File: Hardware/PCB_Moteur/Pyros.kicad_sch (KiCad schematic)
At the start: 33 parts, among them J1 Screw_Terminal_01x04, U3 SI5442DU-T1-GE3, U7 SI5442DU-T1-GE3, U8 LM393

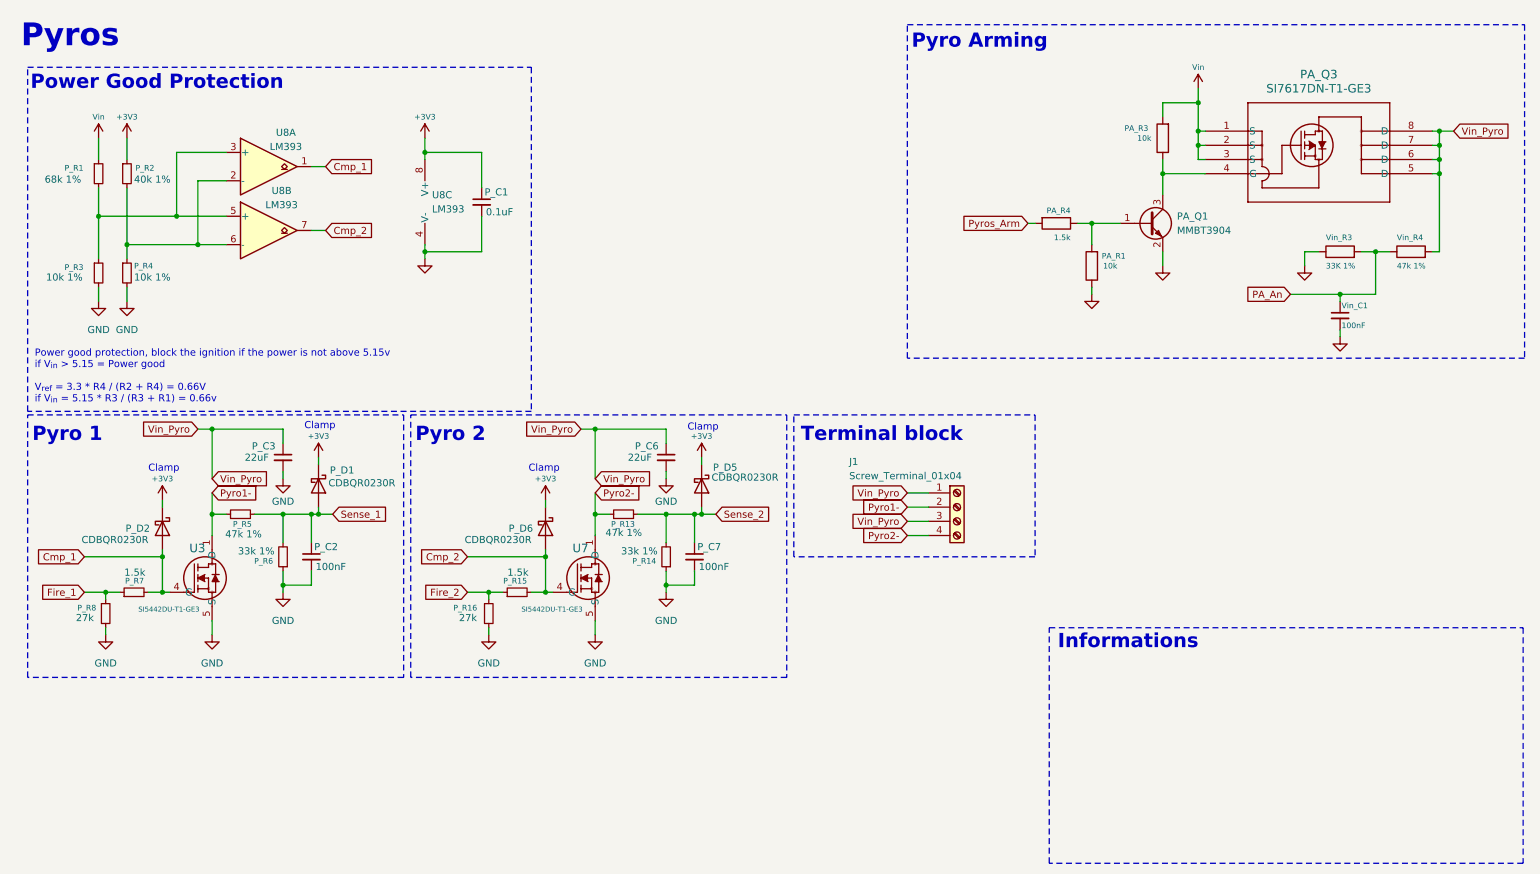
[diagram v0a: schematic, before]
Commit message: fix: LDO 5V SHDN + REFs (missing) + change EN valves controller connection + fix intrumental ampliop + add pull-down to sleep pins
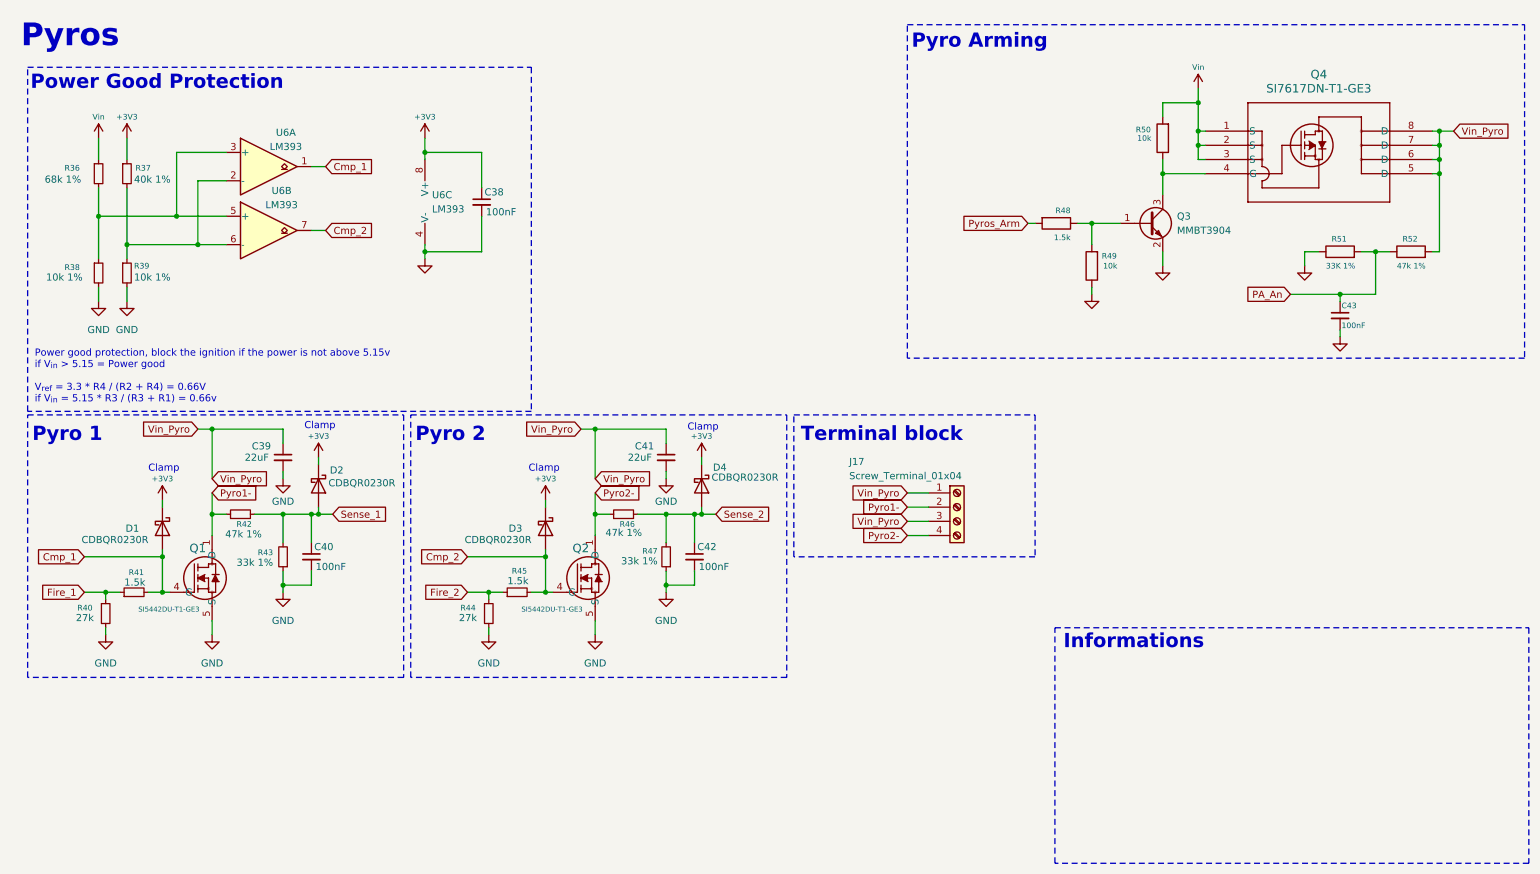
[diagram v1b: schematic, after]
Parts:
- C38: renamed from P_C1; value 0.1uF -> 100nF
- renumbered P_C3 to C39, P_C2 to C40, P_C6 to C41, P_C7 to C42, Vin_C1 to C43, P_D2 to D1, P_D1 to D2, P_D6 to D3, P_D5 to D4, J1 to J17, U3 to Q1, U7 to Q2, PA_Q1 to Q3, PA_Q3 to Q4, P_R1 to R36, P_R2 to R37, P_R3 to R38, P_R4 to R39, P_R8 to R40, P_R7 to R41, P_R5 to R42, P_R6 to R43, P_R16 to R44, P_R15 to R45, P_R13 to R46, P_R14 to R47, PA_R4 to R48, PA_R1 to R49, PA_R3 to R50, Vin_R3 to R51, Vin_R4 to R52, U8 to U6

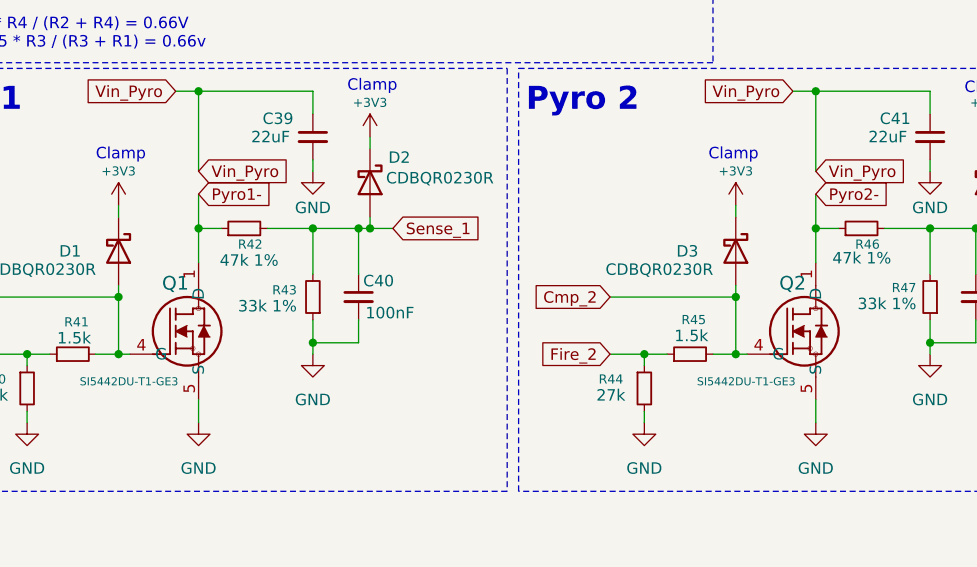
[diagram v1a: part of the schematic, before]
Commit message: wip : minor corrections and fix footprints except connectors
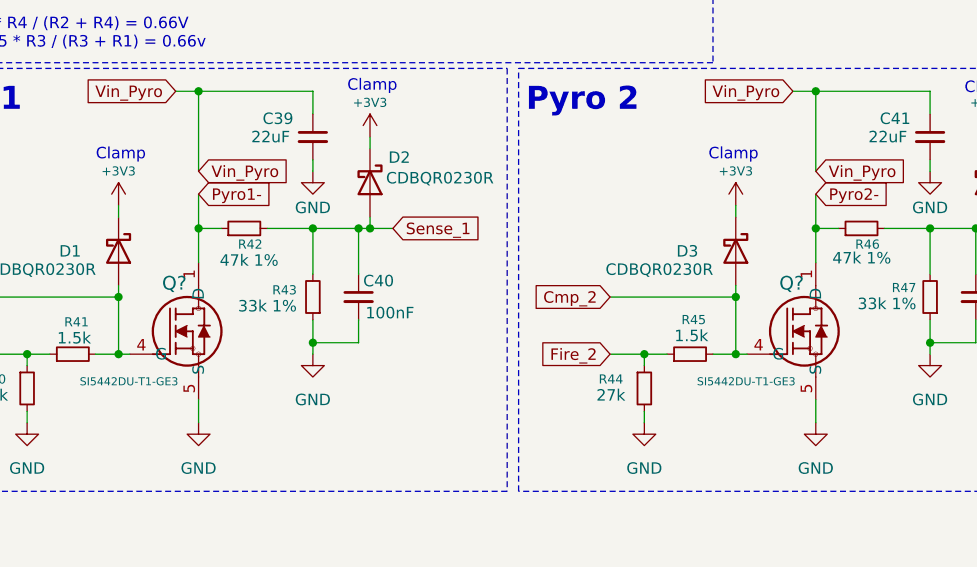
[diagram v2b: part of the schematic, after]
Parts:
- removed Q2: SI5442DU-T1-GE3, SON_8DU-T1-GE3_VIS, symbol ODB2:SI5442DU-T1-GE3
- added Q?: SI5442DU-T1-GE3, pcb_moteur:SON_8DU-T1-GE3_VIS, symbol ODB2:SI5442DU-T1-GE3
- C38, C39, C40, C41, C42, C43: footprint Capacitor_SMD:C_0603_1608Metric -> Capacitor_SMD:C_0805_2012Metric
- Q4: footprint ODB:POWERPAK_1212-8_VIS -> pcb_moteur:POWERPAK_1212-8_VIS
- Q?: renamed from Q1; footprint SON_8DU-T1-GE3_VIS -> pcb_moteur:SON_8DU-T1-GE3_VIS; DigiKey_Part_Number (none) -> SI5442DU-T1-GE3CT-ND; Manufacturer_Part_Number (none) -> SI5442DU-T1-GE3
- U6: footprint (none) -> Package_SO:SOIC-8_3.9x4.9mm_P1.27mm
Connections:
- net Cmp_2: now also Q?.4 (G)
- net GND: now also Q?.5 (S), Q?.9 (S)
- net Pyro2-: now also Q?.1 (D), Q?.10 (D), Q?.2 (D), Q?.3 (D), Q?.6 (D), Q?.7 (D), Q?.8 (D)
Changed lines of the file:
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@@
 	)
 	(symbol
-		(lib_id "ODB2:SI5442DU-T1-GE3")
-		(at 107.95 115.57 0)
-		(unit 1)
-		(exclude_from_sim no)
-		(in_bom yes)
-		(on_board yes)
-		(dnp no)
-		(property "Reference" "Q2"
-			(at 111.506 107.696 0)
-			(effects
-				(font
-					(size 1.524 1.524)
-				)
-				(justify left)
-			)
-		)
-		(property "Value" "SI5442DU-T1-GE3"
-			(at 102.362 118.618 0)
-			(effects
-				(font
-					(size 0.889 0.889)
-				)
-				(justify left)
-			)
-		)
-		(property "Footprint" "SON_8DU-T1-GE3_VIS"
-			(at 107.95 115.57 0)
-			(effects
-				(font
-					(size 1.27 1.27)
-					(italic yes)
-				)
-				(hide yes)
-			)
-		)
-		(property "Datasheet" "https://www.vishay.com/doc?63233"
-			(at 107.95 115.57 0)
-			(effects
-				(font
-					(size 1.27 1.27)
-					(italic yes)
-				)
-				(hide yes)
-			)
-		)
-		(property "Description" ""
-			(at 107.95 115.57 0)
-			(effects
-				(font
-					(size 1.27 1.27)
-				)
-				(hide yes)
-			)
-		)
-		(pin "4"
-		)
-		(pin "2"
-		)
-		(pin "3"
-		)
-		(pin "5"
-		)
-		(pin "1"
-		)
-		(pin "8"
-		)
-		(pin "7"
-		)
-		(pin "9"
-		)
-		(pin "6"
-		)
-		(pin "10"
-		)
-		(instances
-			(project "PCB_moteur"
-				(path "/b0d87684-7b1c-41d8-8358-755aa327573e/1c3f73a9-ace7-4654-9081-04f4c5cd0c08"
-					(reference "Q2")
-					(unit 1)
-				)
-			)
-		)
-	)
-	(symbol
 		(lib_id "power:GND")
 		(at 85.09 55.88 0)
@@
 			)
 		)
-		(property "Footprint" "Capacitor_SMD:C_0603_1608Metric"
+		(property "Footprint" "Capacitor_SMD:C_0805_2012Metric"
 			(at 59.69 91.44 0)
 			(effects
@@
 			)
 		)
-		(property "Footprint" "Capacitor_SMD:C_0603_1608Metric"
+		(property "Footprint" "Capacitor_SMD:C_0805_2012Metric"
 			(at 133.35 109.22 0)
 			(effects
@@
 			)
 		)
-		(property "Footprint" ""
+		(property "Footprint" "Package_SO:SOIC-8_3.9x4.9mm_P1.27mm"
 			(at 57.15 50.8 0)
 			(effects
@@
 			)
 		)
-		(property "Datasheet" "http://www.ti.com/lit/ds/symlink/lm393.pdf"
+		(property "Datasheet" "https://www.digikey.ca/en/products/detail/texas-instruments/LM393DR/276659"
 			(at 57.15 50.8 0)
 			(effects
@@
 			)
 		)
-		(property "Footprint" "Capacitor_SMD:C_0603_1608Metric"
+		(property "Footprint" "Capacitor_SMD:C_0805_2012Metric"
 			(at 248.92 66.04 0)
 			(effects
@@
 			)
 		)
-		(property "Footprint" ""
+		(property "Footprint" "Package_SO:SOIC-8_3.9x4.9mm_P1.27mm"
 			(at 57.15 39.37 0)
 			(effects
@@
 			)
 		)
-		(property "Datasheet" "http://www.ti.com/lit/ds/symlink/lm393.pdf"
+		(property "Datasheet" "https://www.digikey.ca/en/products/detail/texas-instruments/LM393DR/276659"
 			(at 57.15 39.37 0)
 			(effects
@@
 			)
 		)
-		(property "Footprint" "ODB:POWERPAK_1212-8_VIS"
+		(property "Footprint" "pcb_moteur:POWERPAK_1212-8_VIS"
 			(at 224.79 33.02 0)
 			(effects
@@
 			)
 		)
-		(property "Footprint" "Capacitor_SMD:C_0603_1608Metric"
+		(property "Footprint" "Capacitor_SMD:C_0805_2012Metric"
 			(at 64.77 109.22 0)
 			(effects
@@
 			)
 		)
-		(property "Footprint" ""
+		(property "Footprint" "Package_SO:SOIC-8_3.9x4.9mm_P1.27mm"
 			(at 87.63 45.72 0)
 			(effects
@@
 			)
 		)
-		(property "Datasheet" "http://www.ti.com/lit/ds/symlink/lm393.pdf"
+		(property "Datasheet" "https://www.digikey.ca/en/products/detail/texas-instruments/LM393DR/276659"
 			(at 87.63 45.72 0)
 			(effects
@@
 			)
 		)
-		(property "Footprint" "Capacitor_SMD:C_0603_1608Metric"
+		(property "Footprint" "Capacitor_SMD:C_0805_2012Metric"
 			(at 128.27 91.44 0)
 			(effects
@@
 		(lib_name "SI5442DU-T1-GE3_3")
 		(lib_id "ODB2:SI5442DU-T1-GE3")
+		(at 107.95 115.57 0)
+		(unit 1)
+		(exclude_from_sim no)
+		(in_bom yes)
+		(on_board yes)
+		(dnp no)
+		(property "Reference" "Q?"
+			(at 111.506 107.696 0)
+			(effects
+				(font
+					(size 1.524 1.524)
+				)
+				(justify left)
+			)
+		)
+		(property "Value" "SI5442DU-T1-GE3"
+			(at 102.362 118.618 0)
+			(effects
+				(font
+					(size 0.889 0.889)
+				)
+				(justify left)
+			)
+		)
+		(property "Footprint" "pcb_moteur:SON_8DU-T1-GE3_VIS"
+			(at 107.95 115.57 0)
+			(effects
+				(font
+					(size 1.27 1.27)
+					(italic yes)
+				)
+				(hide yes)
+			)
+		)
+		(property "Datasheet" "https://www.digikey.com/en/products/detail/vishay-siliconix/SI5442DU-T1-GE3/4142130"
+			(at 107.95 115.57 0)
+			(effects
+				(font
+					(size 1.27 1.27)
+					(italic yes)
+				)
+				(hide yes)
+			)
+		)
+		(property "Description" ""
+			(at 107.95 115.57 0)
+			(effects
+				(font
+					(size 1.27 1.27)
+				)
+				(hide yes)
+			)
+		)
+		(property "DigiKey_Part_Number" "SI5442DU-T1-GE3CT-ND"
+			(at 107.95 115.57 0)
+			(effects
+				(font
+					(size 1.27 1.27)
+				)
+				(hide yes)
+			)
+		)
+		(property "Purchase-URL" ""
+			(at 107.95 115.57 0)
+			(effects
+				(font
+					(size 1.27 1.27)
+				)
+				(hide yes)
+			)
+		)
+		(property "Sim.Device" ""
+			(at 107.95 115.57 0)
+			(effects
+				(font
+					(size 1.27 1.27)
+				)
+				(hide yes)
+			)
+		)
+		(property "Sim.Pins" ""
+			(at 107.95 115.57 0)
+			(effects
+				(font
+					(size 1.27 1.27)
+				)
+				(hide yes)
+			)
+		)
+		(property "Sim.Type" ""
+			(at 107.95 115.57 0)
+			(effects
+				(font
+					(size 1.27 1.27)
+				)
+				(hide yes)
+			)
+		)
+		(property "Manufacturer_Part_Number" "SI5442DU-T1-GE3"
+			(at 107.95 115.57 0)
+			(effects
+				(font
+					(size 1.27 1.27)
+				)
+				(hide yes)
+			)
+		)
+		(pin "4"
+		)
+		(pin "2"
+		)
+		(pin "3"
+		)
+		(pin "5"
+		)
+		(pin "1"
+		)
+		(pin "8"
+		)
+		(pin "7"
+		)
+		(pin "9"
+		)
+		(pin "6"
+		)
+		(pin "10"
+		)
+		(instances
+			(project "PCB_moteur"
+				(path "/b0d87684-7b1c-41d8-8358-755aa327573e/1c3f73a9-ace7-4654-9081-04f4c5cd0c08"
+					(reference "Q?")
+					(unit 1)
+				)
+			)
+		)
+	)
+	(symbol
+		(lib_name "SI5442DU-T1-GE3_3")
+		(lib_id "ODB2:SI5442DU-T1-GE3")
 		(at 39.37 115.57 0)
 		(unit 1)
@@
 		(on_board yes)
 		(dnp no)
-		(property "Reference" "Q1"
+		(property "Reference" "Q?"
 			(at 42.926 107.696 0)
 			(effects
@@
 			)
 		)
-		(property "Footprint" "SON_8DU-T1-GE3_VIS"
+		(property "Footprint" "pcb_moteur:SON_8DU-T1-GE3_VIS"
 			(at 39.37 115.57 0)
 			(effects
@@
 			)
 		)
-		(property "Datasheet" "https://www.vishay.com/doc?63233"
+		(property "Datasheet" "https://www.digikey.com/en/products/detail/vishay-siliconix/SI5442DU-T1-GE3/4142130"
 			(at 39.37 115.57 0)
 			(effects
@@
 			)
 		)
+		(property "DigiKey_Part_Number" "SI5442DU-T1-GE3CT-ND"
+			(at 39.37 115.57 0)
+			(effects
+				(font
+					(size 1.27 1.27)
+				)
+				(hide yes)
+			)
+		)
+		(property "Purchase-URL" ""
+			(at 39.37 115.57 0)
+			(effects
+				(font
+					(size 1.27 1.27)
+				)
+				(hide yes)
+			)
+		)
+		(property "Sim.Device" ""
+			(at 39.37 115.57 0)
+			(effects
+				(font
+					(size 1.27 1.27)
+				)
+				(hide yes)
+			)
+		)
+		(property "Sim.Pins" ""
+			(at 39.37 115.57 0)
+			(effects
+				(font
+					(size 1.27 1.27)
+				)
+				(hide yes)
+			)
+		)
+		(property "Sim.Type" ""
+			(at 39.37 115.57 0)
+			(effects
+				(font
+					(size 1.27 1.27)
+				)
+				(hide yes)
+			)
+		)
+		(property "Manufacturer_Part_Number" "SI5442DU-T1-GE3"
+			(at 39.37 115.57 0)
+			(effects
+				(font
+					(size 1.27 1.27)
+				)
+				(hide yes)
+			)
+		)
 		(pin "4"
 		)
@@
 			(project "PCB_moteur"
 				(path "/b0d87684-7b1c-41d8-8358-755aa327573e/1c3f73a9-ace7-4654-9081-04f4c5cd0c08"
-					(reference "Q1")
+					(reference "Q?")
 					(unit 1)
 				)
@@
 			)
 		)
-		(property "Footprint" "Capacitor_SMD:C_0603_1608Metric"
+		(property "Footprint" "Capacitor_SMD:C_0805_2012Metric"
 			(at 95.25 45.72 0)
 			(effects

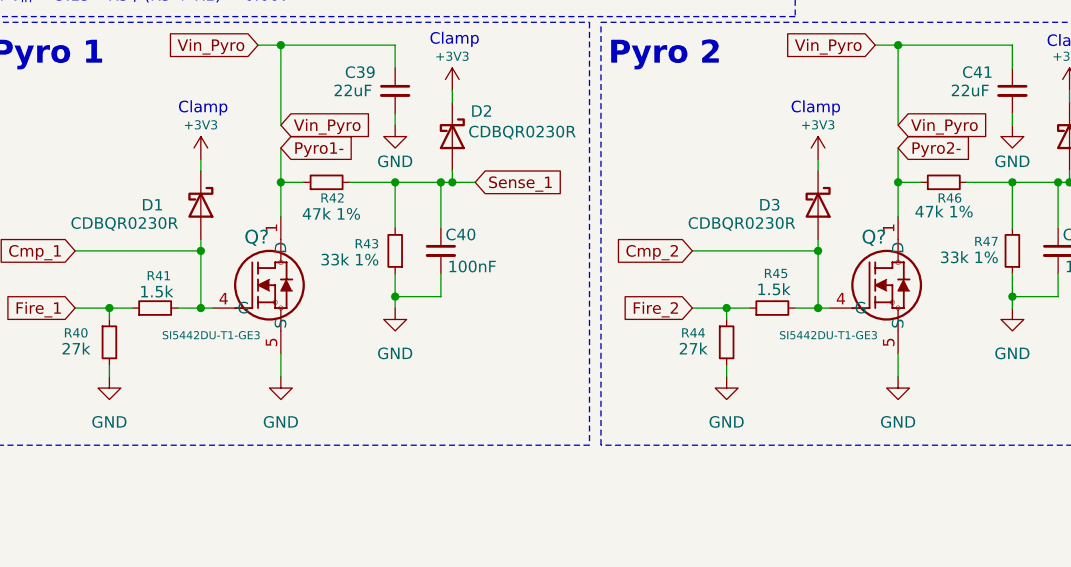
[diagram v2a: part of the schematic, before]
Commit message: fix: symbols refactorisation (footprint missing)
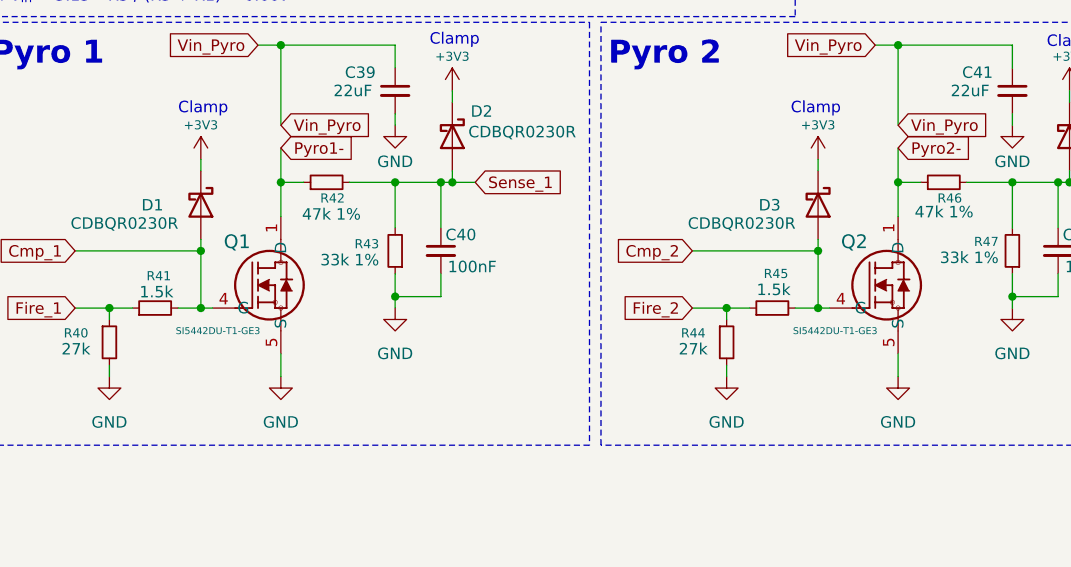
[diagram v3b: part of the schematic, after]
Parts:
- removed Q4: SI7617DN-T1-GE3, pcb_moteur:POWERPAK_1212-8_VIS, symbol ODB2:SI7617DN-T1-GE3
- removed Q? (x2): SI5442DU-T1-GE3, pcb_moteur:SON_8DU-T1-GE3_VIS, symbol ODB2:SI5442DU-T1-GE3
- added Q1, Q2: SI5442DU-T1-GE3, SON_8DU-T1-GE3_VIS, symbol pcb_moteur:SI5442DU-T1-GE3
- added Q4: SI7617DN-T1-GE3, POWERPAK_1212-8_VIS, symbol pcb_moteur:SI7617DN-T1-GE3
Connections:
- net Cmp_1: now also Q1.4 (G)
- net Cmp_2: now also Q2.4 (G)
- net GND: now also Q1.5 (S), Q2.5 (S)
- net Pyro1-: now also Q1.1 (D)
- net Pyro2-: now also Q2.1 (D)
- net Vin: now also Q4.1 (S), Q4.2 (S), Q4.3 (S)
- net Vin_Pyro: now also Q4.5 (D), Q4.6 (D), Q4.7 (D), Q4.8 (D)
- net at Q3.3 (C), R50.1: now also Q4.4 (G)

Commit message: wip : done all footprints
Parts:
- J17: footprint (none) -> pcb_moteur:CONN_OSTVN04A150_OST
- Q1, Q2: footprint SON_8DU-T1-GE3_VIS -> pcb_moteur:SI5442DU_T1_G3
- Q4: footprint POWERPAK_1212-8_VIS -> pcb_moteur:SI7617DN-T1-GE3
- R49, R50: footprint Resistor_SMD:R_0603_1608Metric -> Resistor_SMD:R_0805_2012Metric
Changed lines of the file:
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@@
 			)
 		)
-		(property "Footprint" "Resistor_SMD:R_0603_1608Metric"
+		(property "Footprint" "Resistor_SMD:R_0805_2012Metric"
 			(at 218.948 34.29 90)
 			(effects
@@
 			)
 		)
-		(property "Footprint" "Resistor_SMD:R_0603_1608Metric"
+		(property "Footprint" "Resistor_SMD:R_0805_2012Metric"
 			(at 206.248 57.15 90)
 			(effects
@@
 			)
 		)
-		(property "Footprint" "SON_8DU-T1-GE3_VIS"
+		(property "Footprint" "pcb_moteur:SI5442DU_T1_G3"
 			(at 113.03 133.096 0)
 			(effects
@@
 			)
 		)
-		(property "Footprint" "POWERPAK_1212-8_VIS"
+		(property "Footprint" "pcb_moteur:SI7617DN-T1-GE3"
 			(at 224.79 33.02 0)
 			(effects
@@
 			)
 		)
-		(property "Footprint" "SON_8DU-T1-GE3_VIS"
+		(property "Footprint" "pcb_moteur:SI5442DU_T1_G3"
 			(at 44.45 133.096 0)
 			(effects
@@
 			)
 		)
-		(property "Footprint" ""
+		(property "Footprint" "pcb_moteur:CONN_OSTVN04A150_OST"
 			(at 180.34 100.33 0)
 			(effects
@@
 			)
 		)
-		(property "Datasheet" "~"
+		(property "Datasheet" "https://www.digikey.ca/en/products/detail/on-shore-technology-inc/OSTVN04A150/1588864"
 			(at 180.34 100.33 0)
 			(effects
